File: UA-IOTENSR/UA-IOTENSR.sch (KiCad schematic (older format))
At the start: 2 parts, among them SW1 SW_MEC_5G, U1 ESP32-S2-WROOM

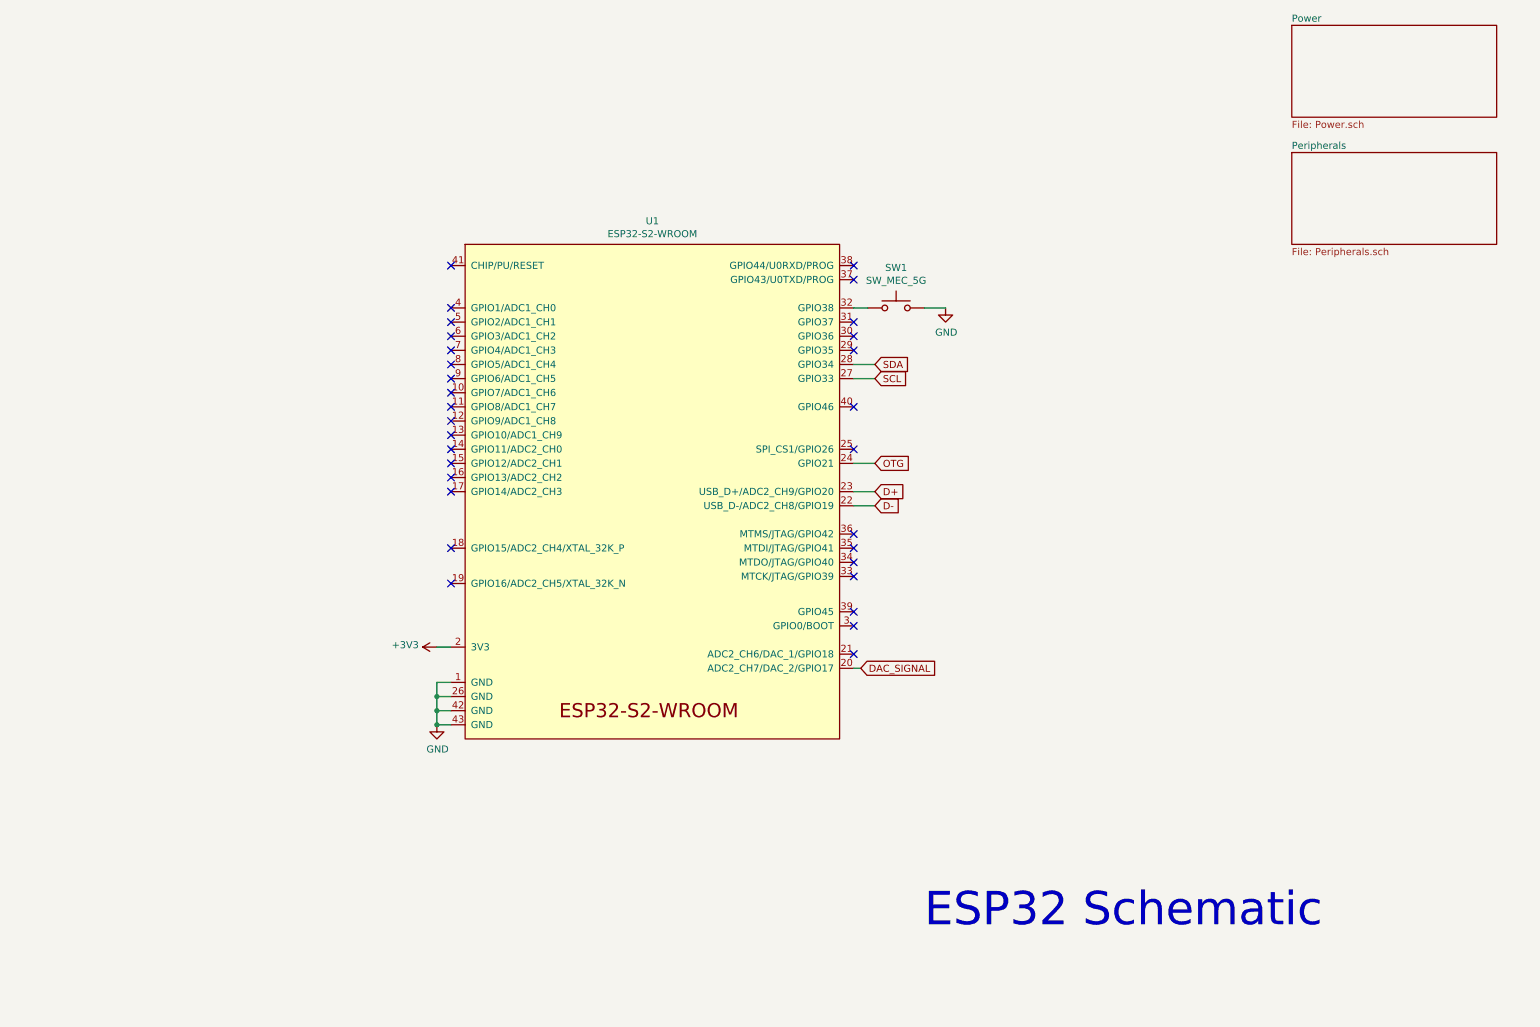
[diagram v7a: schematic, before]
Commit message: Organized ESP32 main schem
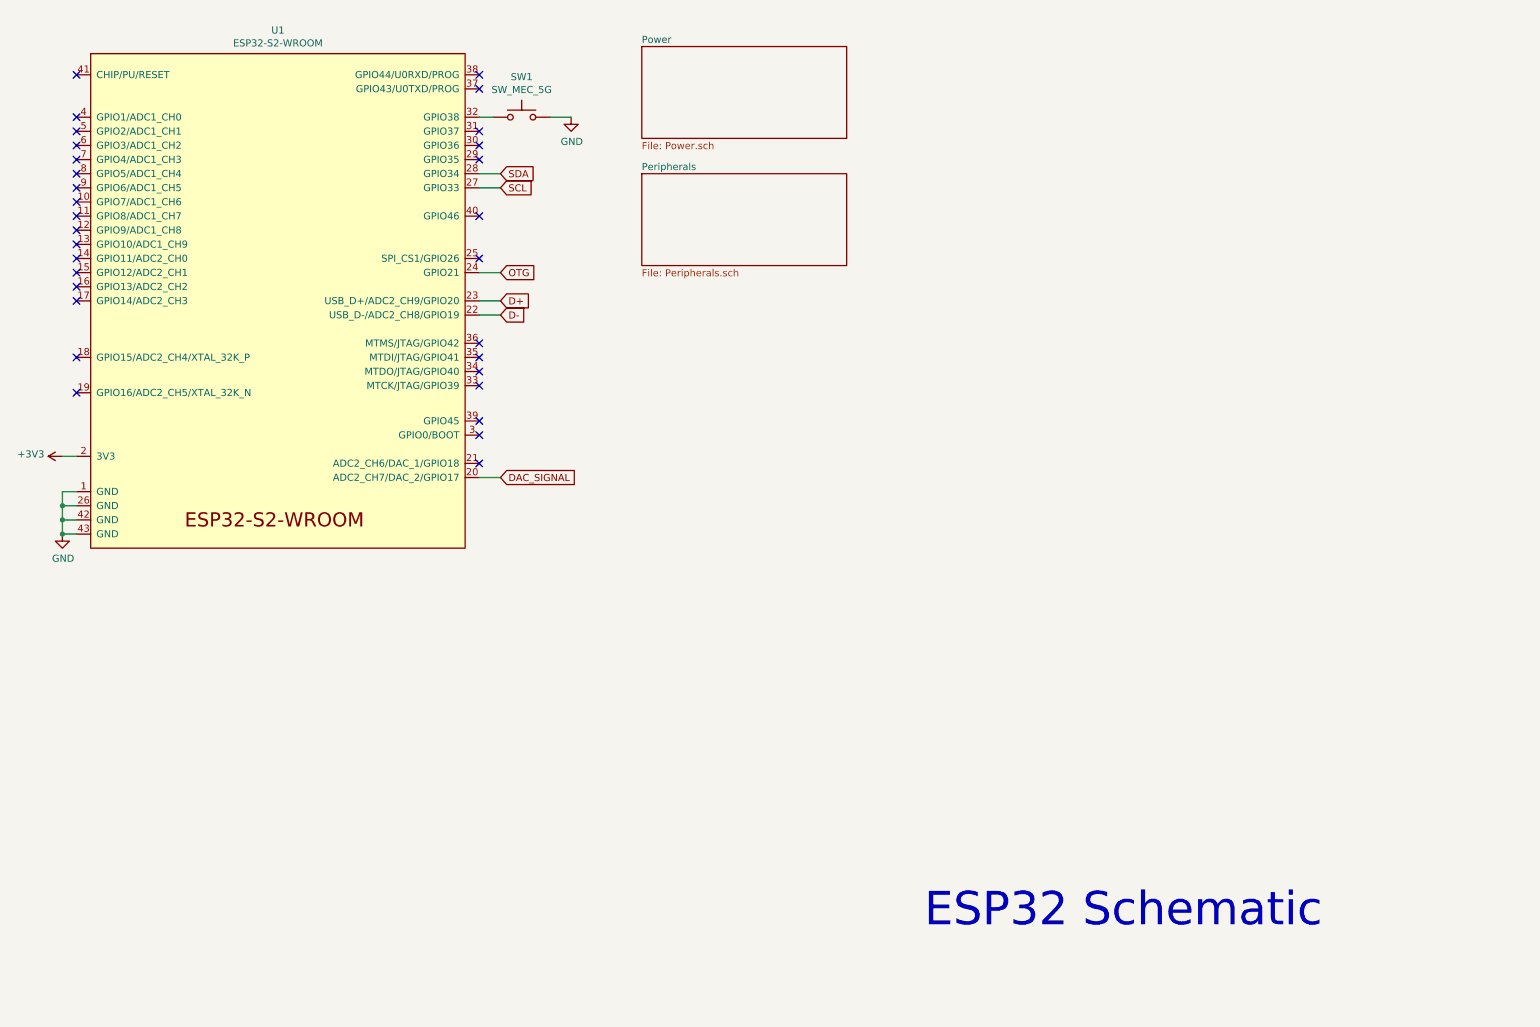
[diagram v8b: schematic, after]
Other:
- moved on the sheet: SW1, U1
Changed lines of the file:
@@
 L power:GND #PWR01
 U 1 1 61961638
-P 3550 5550
-F 0 "#PWR01" H 3550 5300 50  0001 C CNN
-F 1 "GND" H 3555 5377 50  0000 C CNN
-F 2 "" H 3550 5550 50  0001 C CNN
-F 3 "" H 3550 5550 50  0001 C CNN
-	1    3550 5550
+P 900 4200
+F 0 "#PWR01" H 900 3950 50  0001 C CNN
+F 1 "GND" H 905 4027 50  0000 C CNN
+F 2 "" H 900 4200 50  0001 C CNN
+F 3 "" H 900 4200 50  0001 C CNN
+	1    900  4200
 	1    0    0    -1
 $EndComp
 Wire Wire Line
-	3550 5350 3650 5350
+	900  4000 1000 4000
 Wire Wire Line
-	3550 5450 3650 5450
+	900  4100 1000 4100
 Wire Wire Line
-	3550 5550 3650 5550
+	900  4200 1000 4200
 $Comp
 L Espressif:ESP32-S2-WROOM U1
 U 1 1 619E5D94
-P 5050 3900
-F 0 "U1" H 5075 5815 50  0000 C CNN
-F 1 "ESP32-S2-WROOM" H 5075 5724 50  0000 C CNN
-F 2 "Espressif:ESP32-S2-WROOM" H 5050 2000 50  0001 C CNN
-F 3 "https://www.espressif.com/sites/default/files/documentation/esp32-s2-wroom_esp32-s2-wroom-i_datasheet_en.pdf" H 5050 3900 50  0001 C CNN
-	1    5050 3900
+P 2400 2550
+F 0 "U1" H 2425 4465 50  0000 C CNN
+F 1 "ESP32-S2-WROOM" H 2425 4374 50  0000 C CNN
+F 2 "Espressif:ESP32-S2-WROOM" H 2400 650 50  0001 C CNN
+F 3 "https://www.espressif.com/sites/default/files/documentation/esp32-s2-wroom_esp32-s2-wroom-i_datasheet_en.pdf" H 2400 2550 50  0001 C CNN
+	1    2400 2550
 	1    0    0    -1
 $EndComp
 Wire Wire Line
-	3650 5250 3550 5250
+	1000 3900 900  3900
 Wire Wire Line
-	3550 5250 3550 5350
-Connection ~ 3550 5350
+	900  3900 900  4000
+Connection ~ 900  4000
 Wire Wire Line
-	3550 5350 3550 5450
-Connection ~ 3550 5450
+	900  4000 900  4100
+Connection ~ 900  4100
 Wire Wire Line
-	3550 5450 3550 5550
-Connection ~ 3550 5550
+	900  4100 900  4200
+Connection ~ 900  4200
 Wire Wire Line
-	6500 3100 6650 3100
-Text GLabel 6650 3100 2    50   Input ~ 0
+	3850 1750 4000 1750
+Text GLabel 4000 1750 2    50   Input ~ 0
 SCL
-Text GLabel 6650 3000 2    50   Input ~ 0
+Text GLabel 4000 1650 2    50   Input ~ 0
 SDA
 Wire Wire Line
-	6500 3000 6650 3000
+	3850 1650 4000 1650
 Wire Wire Line
-	7000 2600 7150 2600
+	4350 1250 4500 1250
 $Comp
 L Switch:SW_MEC_5G SW1
 U 1 1 619D98CD
-P 6800 2600
-F 0 "SW1" H 6800 2885 50  0000 C CNN
-F 1 "SW_MEC_5G" H 6800 2794 50  0000 C CNN
-F 2 "" H 6800 2800 50  0001 C CNN
-F 3 "http://www.apem.com/int/index.php?controller=attachment&id_attachment=488" H 6800 2800 50  0001 C CNN
-	1    6800 2600
+P 4150 1250
+F 0 "SW1" H 4150 1535 50  0000 C CNN
+F 1 "SW_MEC_5G" H 4150 1444 50  0000 C CNN
+F 2 "" H 4150 1450 50  0001 C CNN
+F 3 "http://www.apem.com/int/index.php?controller=attachment&id_attachment=488" H 4150 1450 50  0001 C CNN
+	1    4150 1250
 	1    0    0    -1
 $EndComp
 Wire Wire Line
-	6500 2600 6600 2600
+	3850 1250 3950 1250
 $Comp
 L power:GND #PWR02
 U 1 1 61A04BEB
-P 7150 2600
-F 0 "#PWR02" H 7150 2350 50  0001 C CNN
-F 1 "GND" H 7155 2427 50  0000 C CNN
-F 2 "" H 7150 2600 50  0001 C CNN
-F 3 "" H 7150 2600 50  0001 C CNN
-	1    7150 2600
+P 4500 1250
+F 0 "#PWR02" H 4500 1000 50  0001 C CNN
+F 1 "GND" H 4505 1077 50  0000 C CNN
+F 2 "" H 4500 1250 50  0001 C CNN
+F 3 "" H 4500 1250 50  0001 C CNN
+	1    4500 1250
 	1    0    0    -1
 $EndComp
 Wire Wire Line
-	3650 5000 3550 5000
-Text GLabel 6650 3900 2    50   Input ~ 0
+	1000 3650 900  3650
+Text GLabel 4000 2550 2    50   Input ~ 0
 D+
 Wire Wire Line
-	6500 3900 6650 3900
-Text GLabel 6650 4000 2    50   Input ~ 0
+	3850 2550 4000 2550
+Text GLabel 4000 2650 2    50   Input ~ 0
 D-
 Wire Wire Line
-	6500 4000 6650 4000
+	3850 2650 4000 2650
 Wire Wire Line
-	6500 3700 6650 3700
-Text GLabel 6650 3700 2    50   Input ~ 0
+	3850 2350 4000 2350
+Text GLabel 4000 2350 2    50   Input ~ 0
 OTG
 $Sheet
-S 9600 600  1450 650
+S 5000 750  1450 650
 U 61A2F8E2
 F0 "Power" 50
 F1 "Power.sch" 50
 $EndSheet
-NoConn ~ 6500 5050
-NoConn ~ 6500 4850
-NoConn ~ 6500 4750
-NoConn ~ 6500 4500
-NoConn ~ 6500 4400
-NoConn ~ 6500 4300
-NoConn ~ 6500 4200
-NoConn ~ 6500 3600
-NoConn ~ 6500 3300
-NoConn ~ 6500 2900
-NoConn ~ 6500 2800
-NoConn ~ 6500 2700
-NoConn ~ 6500 2400
-NoConn ~ 6500 2300
-NoConn ~ 3650 2300
-NoConn ~ 3650 2600
-NoConn ~ 3650 2700
-NoConn ~ 3650 2800
-NoConn ~ 3650 2900
-NoConn ~ 3650 3000
-NoConn ~ 3650 3100
-NoConn ~ 3650 3200
-NoConn ~ 3650 3300
-NoConn ~ 3650 3400
-NoConn ~ 3650 3500
-NoConn ~ 3650 3600
-NoConn ~ 3650 3700
-NoConn ~ 3650 3800
-NoConn ~ 3650 3900
-NoConn ~ 3650 4300
-NoConn ~ 3650 4550
-Wire Wire Line
-	6500 5150 6550 5150
+NoConn ~ 3850 3700
+NoConn ~ 3850 3500
+NoConn ~ 3850 3400
+NoConn ~ 3850 3150
+NoConn ~ 3850 3050
+NoConn ~ 3850 2950
+NoConn ~ 3850 2850
+NoConn ~ 3850 2250
+NoConn ~ 3850 1950
+NoConn ~ 3850 1550
+NoConn ~ 3850 1450
+NoConn ~ 3850 1350
+NoConn ~ 3850 1050
+NoConn ~ 3850 950
+NoConn ~ 1000 950
+NoConn ~ 1000 1250
+NoConn ~ 1000 1350
+NoConn ~ 1000 1450
+NoConn ~ 1000 1550
+NoConn ~ 1000 1650
+NoConn ~ 1000 1750
+NoConn ~ 1000 1850
+NoConn ~ 1000 1950
+NoConn ~ 1000 2050
+NoConn ~ 1000 2150
+NoConn ~ 1000 2250
+NoConn ~ 1000 2350
+NoConn ~ 1000 2450
+NoConn ~ 1000 2550
+NoConn ~ 1000 2950
+NoConn ~ 1000 3200
 $Sheet
-S 9600 1500 1450 650
+S 5000 1650 1450 650
 U 61A1DC3C
 F0 "Peripherals" 50
@@
 L power:+3V3 #PWR06
 U 1 1 61A18D2A
-P 3550 5000
-F 0 "#PWR06" H 3550 4850 50  0001 C CNN
-F 1 "+3V3" V 3565 5128 50  0000 L CNN
-F 2 "" H 3550 5000 50  0001 C CNN
-F 3 "" H 3550 5000 50  0001 C CNN
-	1    3550 5000
+P 900 3650
+F 0 "#PWR06" H 900 3500 50  0001 C CNN
+F 1 "+3V3" V 915 3778 50  0000 L CNN
+F 2 "" H 900 3650 50  0001 C CNN
+F 3 "" H 900 3650 50  0001 C CNN
+	1    900  3650
 	0    -1   -1   0
 $EndComp
-Text GLabel 6550 5150 2    50   Input ~ 0
+Text GLabel 4000 3800 2    50   Input ~ 0
 DAC_SIGNAL
+Wire Wire Line
+	3850 3800 4000 3800
 $EndSCHEMATC
